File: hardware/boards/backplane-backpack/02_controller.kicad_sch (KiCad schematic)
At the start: 12 parts, among them J10 SWD (TBD), U1 STM32C092FCP6

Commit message: chore: checkpoint workspace changes
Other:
- company: (none) -> Karl Quinsland
- title: MCU and Debug -> Backplane Backpack

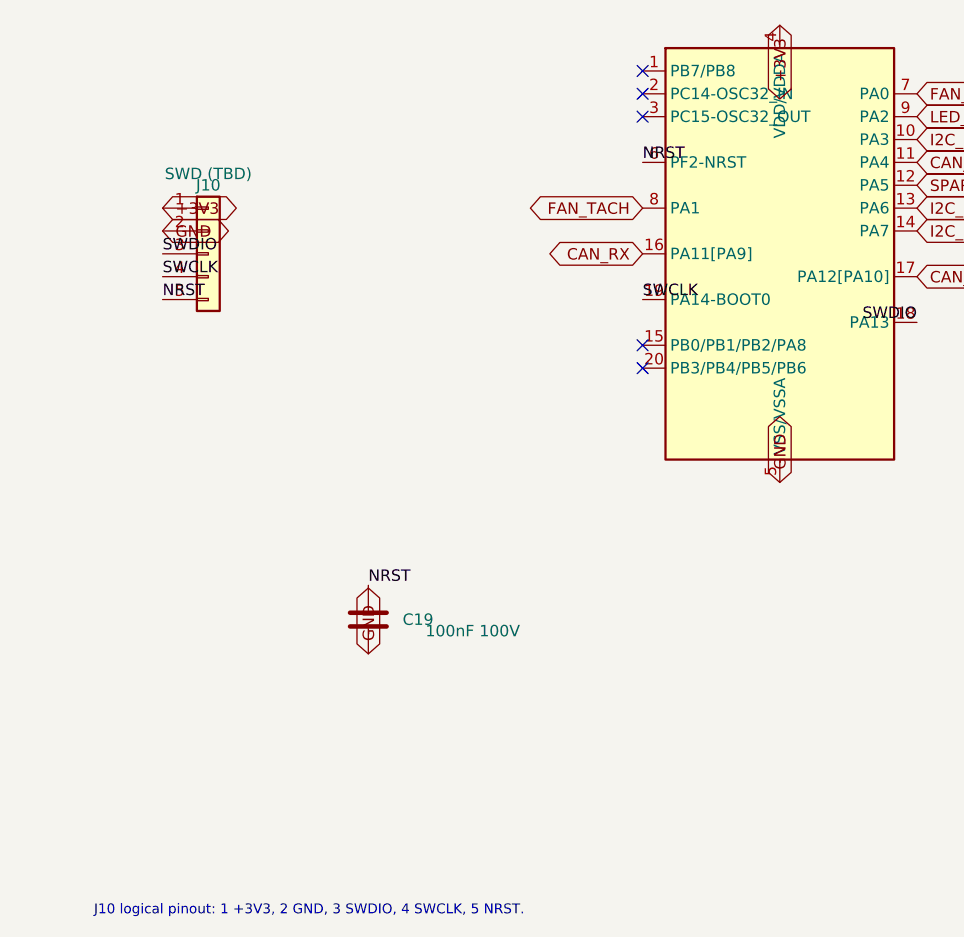
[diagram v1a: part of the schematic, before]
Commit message: fix: normalize power symbols and connector grounds
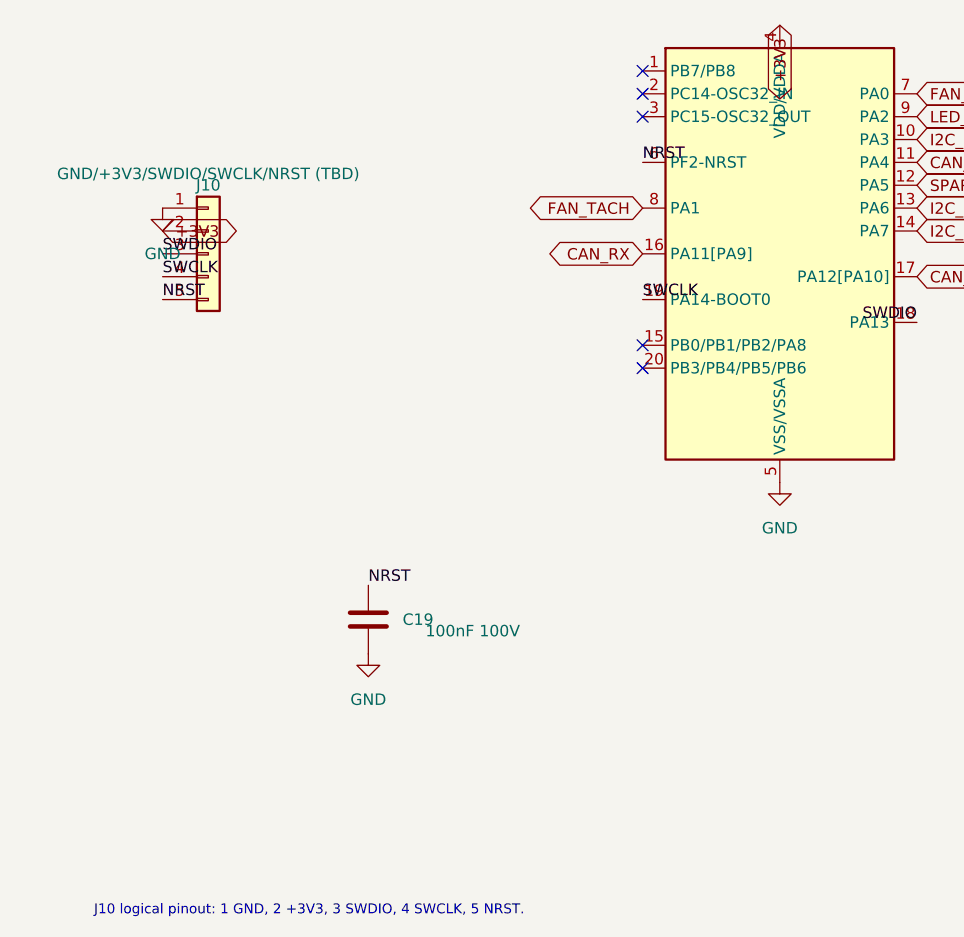
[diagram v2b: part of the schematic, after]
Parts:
- J10: value SWD (TBD) -> GND/+3V3/SWDIO/SWCLK/NRST (TBD)
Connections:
- net +3V3: now also J10.2 (Pin_2); no longer J10.1 (Pin_1)
- net GND: now also J10.1 (Pin_1); no longer J10.2 (Pin_2)
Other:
- note added: "J10 logical pinout: 1 GND, 2 +3V3, 3 SWDIO, 4 SWCLK, 5 NRST."
- note removed: "J10 logical pinout: 1 +3V3, 2 GND, 3 SWDIO, 4 SWCLK, 5 NRST."

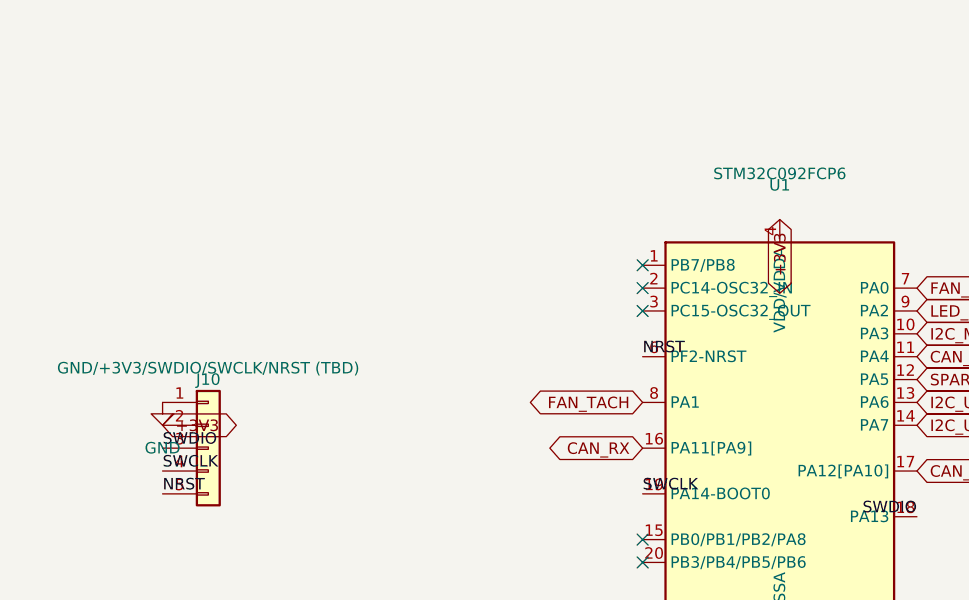
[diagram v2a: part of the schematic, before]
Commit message: fix: standardize +3V3 power symbols
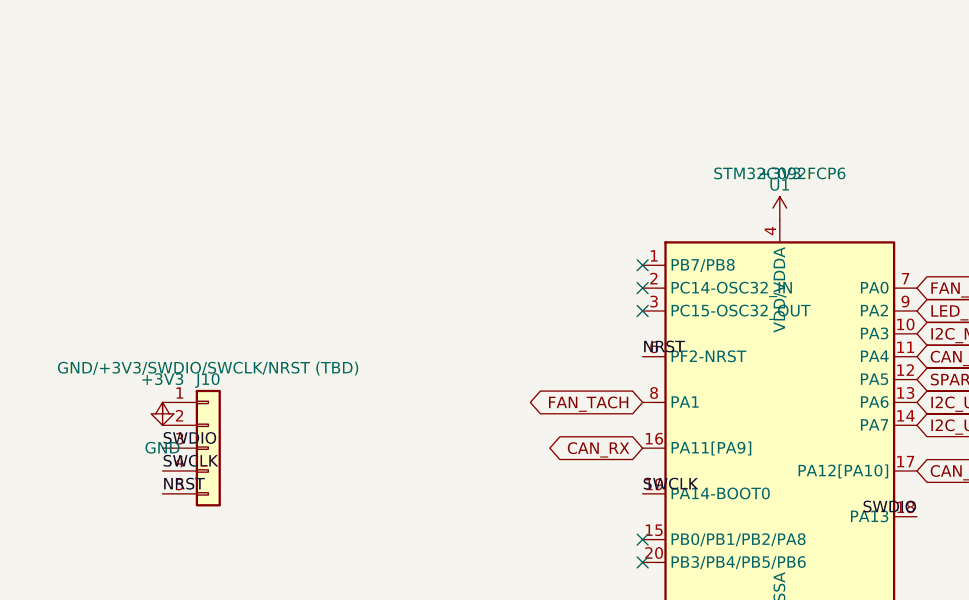
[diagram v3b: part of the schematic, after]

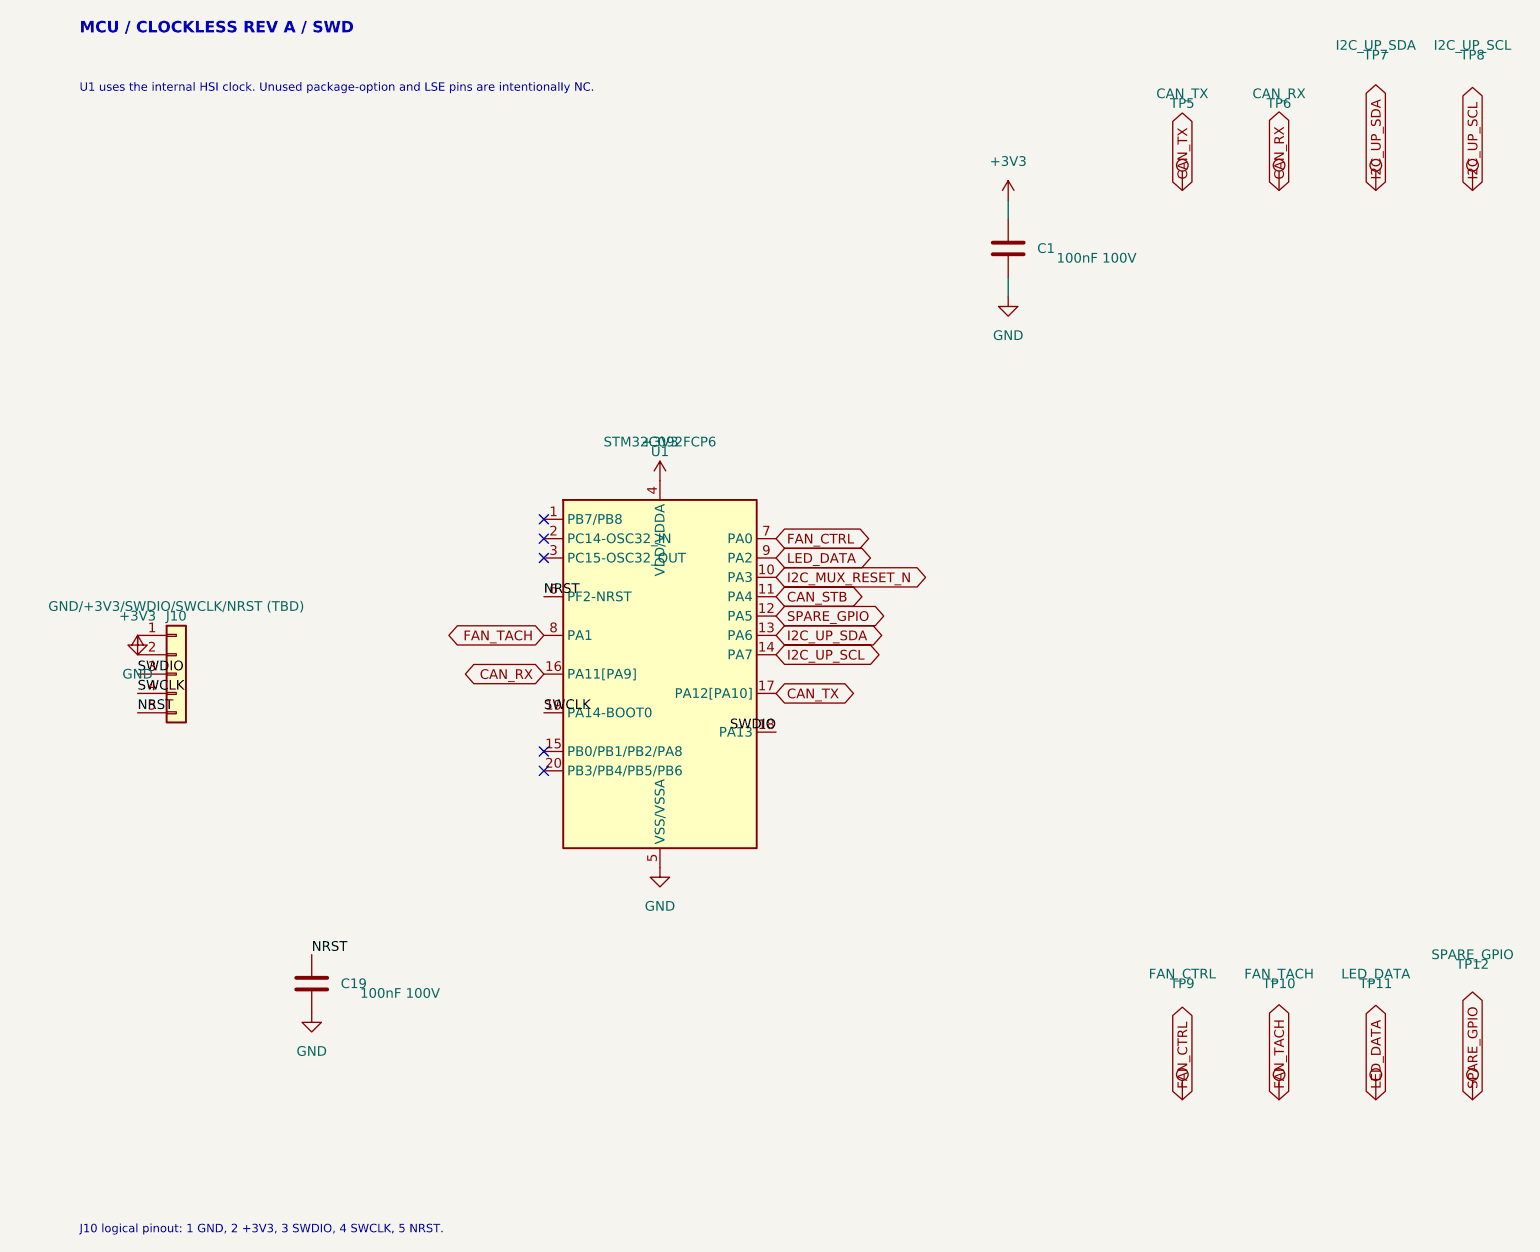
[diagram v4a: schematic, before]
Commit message: feat: connect slot power controls
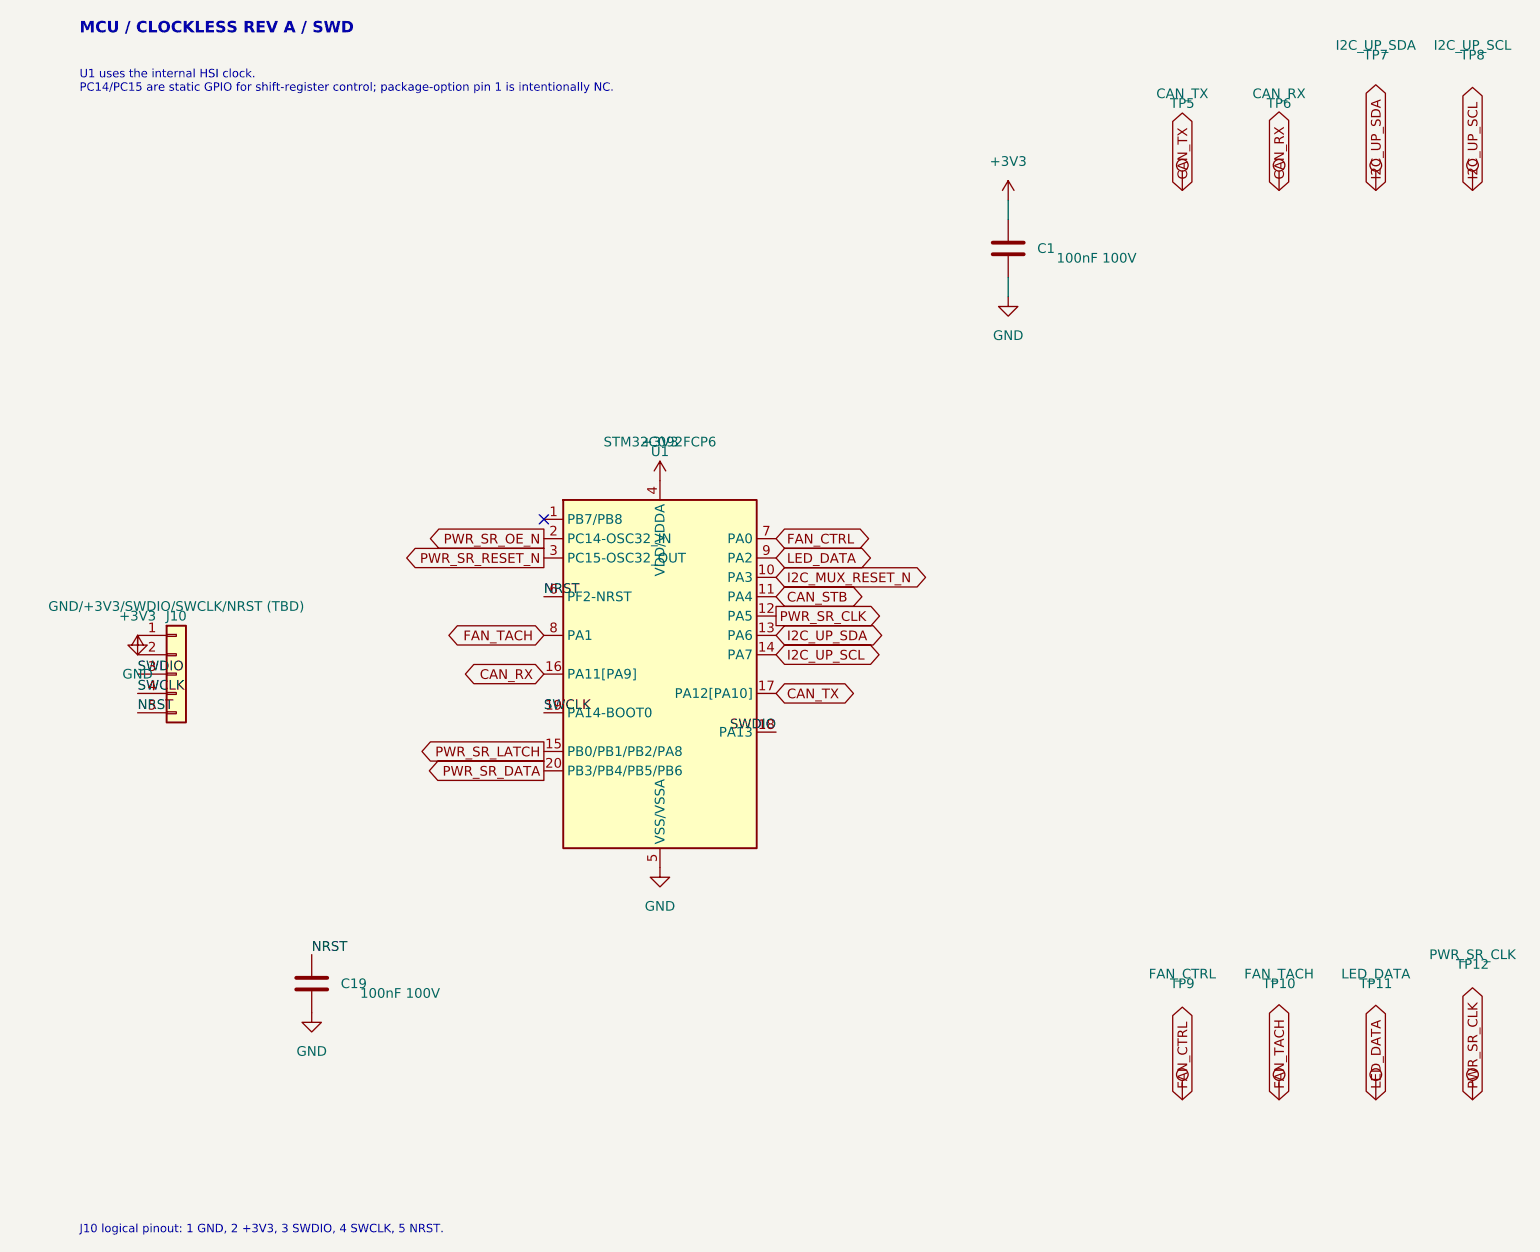
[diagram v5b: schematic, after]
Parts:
- TP12: value SPARE_GPIO -> PWR_SR_CLK
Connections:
- net PWR_SR_LATCH: now reaches U1.15 (PB0/PB1/PB2/PA8)
- net PWR_SR_OE_N: now reaches U1.2 (PC14-OSC32_IN)
- net PWR_SR_DATA: now reaches U1.20 (PB3/PB4/PB5/PB6)
- net PWR_SR_RESET_N: now reaches U1.3 (PC15-OSC32_OUT)
- net SPARE_GPIO renamed PWR_SR_CLK
- no-connect marks 5 -> 1
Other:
- note added: "U1 uses the internal HSI clock. PC14/PC15 are static GPIO for shift-register control; package-option pin 1 is intentionally NC."
- note removed: "U1 uses the internal HSI clock. Unused package-option and LSE pins are intentionally NC."
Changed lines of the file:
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@@
 		)
 	)
-	(text "U1 uses the internal HSI clock. Unused package-option and LSE pins are intentionally NC."
+	(text "U1 uses the internal HSI clock.\nPC14/PC15 are static GPIO for shift-register control; package-option pin 1 is intentionally NC."
 		(exclude_from_sim no)
 		(at 25.4 25.4 0)
@@
 	)
 	(no_connect
-		(at 86.36 83.82)
-	)
-	(no_connect
-		(at 86.36 114.3)
-	)
-	(no_connect
-		(at 86.36 111.76)
-	)
-	(no_connect
 		(at 86.36 81.28)
-	)
-	(no_connect
-		(at 86.36 86.36)
 	)
 	(wire
@@
 		)
 	)
-	(global_label "SPARE_GPIO"
-		(shape bidirectional)
+	(global_label "PWR_SR_OE_N"
+		(shape output)
+		(at 86.36 83.82 180)
+		(effects
+			(font
+				(size 1.27 1.27)
+			)
+			(justify right)
+		)
+		(property "Intersheetrefs" "${INTERSHEET_REFS}"
+			(at 86.36 83.82 0)
+			(hide yes)
+			(show_name no)
+			(do_not_autoplace no)
+			(effects
+				(font
+					(size 1.27 1.27)
+				)
+			)
+		)
+	)
+	(global_label "PWR_SR_RESET_N"
+		(shape output)
+		(at 86.36 86.36 180)
+		(effects
+			(font
+				(size 1.27 1.27)
+			)
+			(justify right)
+		)
+		(property "Intersheetrefs" "${INTERSHEET_REFS}"
+			(at 86.36 86.36 0)
+			(hide yes)
+			(show_name no)
+			(do_not_autoplace no)
+			(effects
+				(font
+					(size 1.27 1.27)
+				)
+			)
+		)
+	)
+	(global_label "PWR_SR_LATCH"
+		(shape output)
+		(at 86.36 111.76 180)
+		(effects
+			(font
+				(size 1.27 1.27)
+			)
+			(justify right)
+		)
+		(property "Intersheetrefs" "${INTERSHEET_REFS}"
+			(at 86.36 111.76 0)
+			(hide yes)
+			(show_name no)
+			(do_not_autoplace no)
+			(effects
+				(font
+					(size 1.27 1.27)
+				)
+			)
+		)
+	)
+	(global_label "PWR_SR_DATA"
+		(shape output)
+		(at 86.36 114.3 180)
+		(effects
+			(font
+				(size 1.27 1.27)
+			)
+			(justify right)
+		)
+		(property "Intersheetrefs" "${INTERSHEET_REFS}"
+			(at 86.36 114.3 0)
+			(hide yes)
+			(show_name no)
+			(do_not_autoplace no)
+			(effects
+				(font
+					(size 1.27 1.27)
+				)
+			)
+		)
+	)
+	(global_label "PWR_SR_CLK"
+		(shape output)
 		(at 116.84 93.98 0)
 		(effects
@@
 		)
 	)
-	(global_label "SPARE_GPIO"
+	(global_label "PWR_SR_CLK"
 		(shape bidirectional)
 		(at 208.28 157.48 90)
@@
 			)
 		)
-		(property "Value" "SPARE_GPIO"
+		(property "Value" "PWR_SR_CLK"
 			(at 208.28 138.43 0)
 			(show_name no)

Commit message: chore: checkpoint current board layout
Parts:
- removed J10: GND/+3V3/SWDIO/SWCLK/NRST (TBD), symbol Connector_Generic:Conn_01x05
- removed TP10: FAN_TACH, TestPoint:TestPoint_Pad_D1.5mm, symbol Connector:TestPoint
- removed TP11: LED_DATA, TestPoint:TestPoint_Pad_D1.5mm, symbol Connector:TestPoint
- removed TP12: PWR_SR_CLK, TestPoint:TestPoint_Pad_D1.5mm, symbol Connector:TestPoint
- removed TP5: CAN_TX, TestPoint:TestPoint_Pad_D1.5mm, symbol Connector:TestPoint
- removed TP6: CAN_RX, TestPoint:TestPoint_Pad_D1.5mm, symbol Connector:TestPoint
- removed TP7: I2C_UP_SDA, TestPoint:TestPoint_Pad_D1.5mm, symbol Connector:TestPoint
- removed TP8: I2C_UP_SCL, TestPoint:TestPoint_Pad_D1.5mm, symbol Connector:TestPoint
- removed TP9: FAN_CTRL, TestPoint:TestPoint_Pad_D1.5mm, symbol Connector:TestPoint
- added J10: SWD, symbol Connector_Generic:Conn_01x06
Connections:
- net +3V3: now also J10.2 (Pin_2)
- net GND: now also J10.1 (Pin_1)
- net NRST: now also J10.5 (Pin_5)
- net PWR_SR_CLK: now also J10.6 (Pin_6)
- net SWCLK: now also J10.4 (Pin_4)
- net SWDIO: now also J10.3 (Pin_3)
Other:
- note added: "TODO: tag-connect or similar?"
- note removed: "J10 logical pinout: 1 GND, 2 +3V3, 3 SWDIO, 4 SWCLK, 5 NRST."
- moved on the sheet: C1, C19
